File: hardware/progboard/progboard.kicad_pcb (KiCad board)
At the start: 2 copper layers, 74.9 x 58.4 mm, 23 parts, among them J1 LEFT, J2 RIGHT, J3 SWD, J4 CV A, J5 POWER

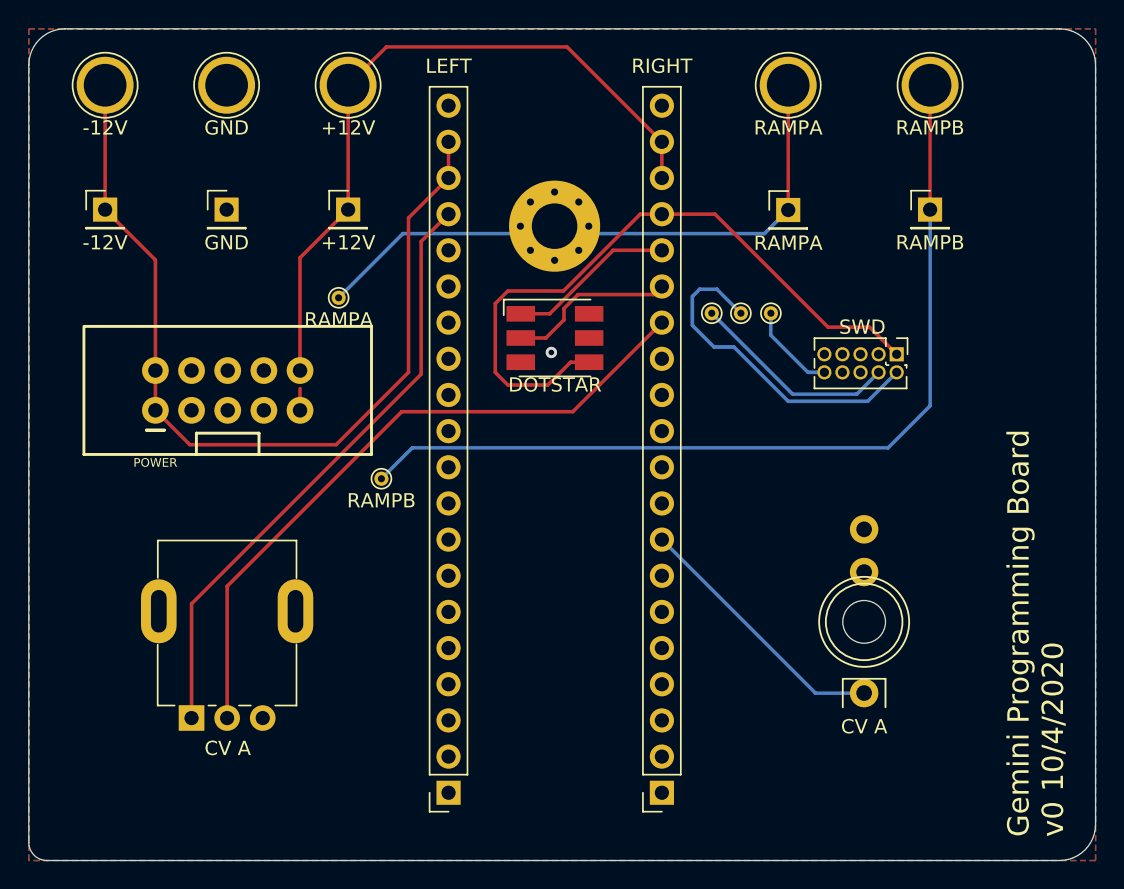
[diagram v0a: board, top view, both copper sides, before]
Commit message: Add LEDs to the progboard
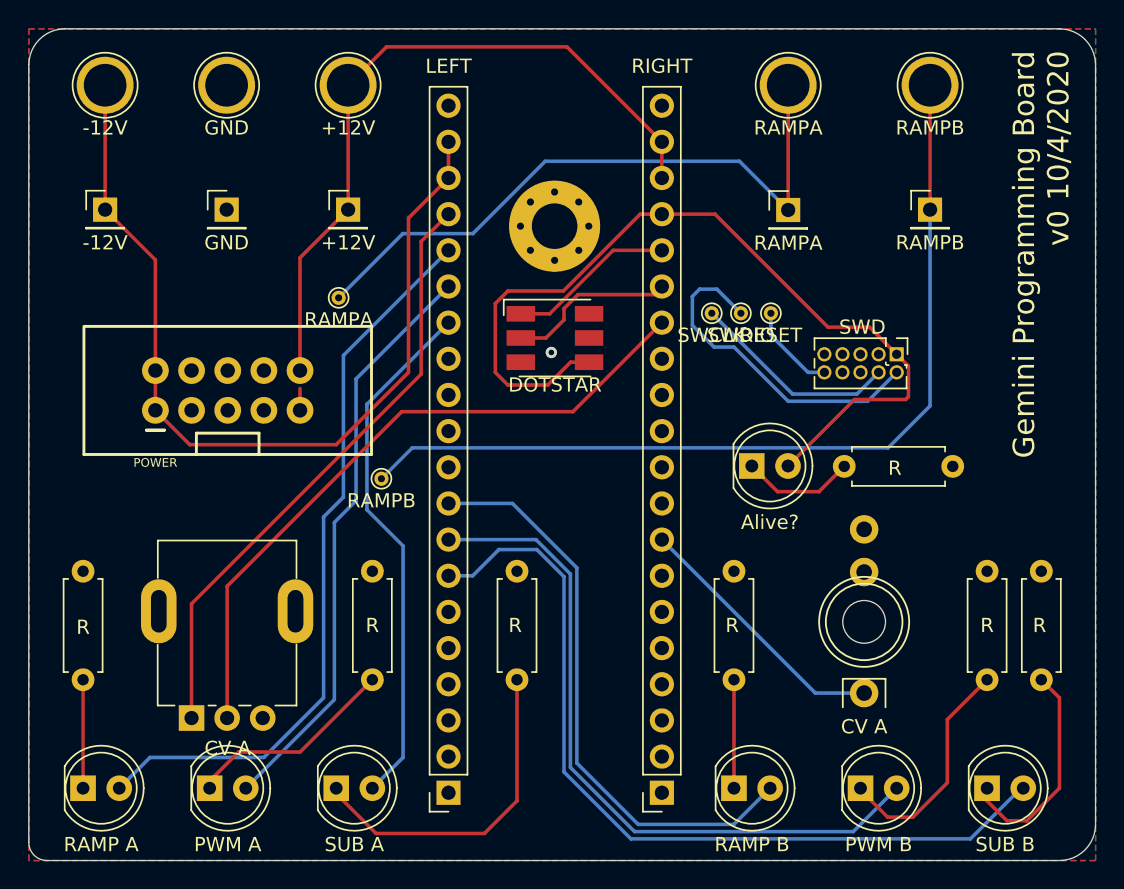
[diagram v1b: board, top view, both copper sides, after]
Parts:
- added 1k1: R, Resistor_THT:R_Axial_DIN0207_L6.3mm_D2.5mm_P7.62mm_Horizontal, F.Cu at (119.4, 108.0)
- added 1k2: R, Resistor_THT:R_Axial_DIN0207_L6.3mm_D2.5mm_P7.62mm_Horizontal, F.Cu at (139.7, 108.0)
- added 1k3: R, Resistor_THT:R_Axial_DIN0207_L6.3mm_D2.5mm_P7.62mm_Horizontal, F.Cu at (149.9, 108.0)
- added 1k4: R, Resistor_THT:R_Axial_DIN0207_L6.3mm_D2.5mm_P7.62mm_Horizontal, F.Cu at (165.1, 108.0)
- added 1k5: R, Resistor_THT:R_Axial_DIN0207_L6.3mm_D2.5mm_P7.62mm_Horizontal, F.Cu at (182.9, 108.0)
- added 1k6: R, Resistor_THT:R_Axial_DIN0207_L6.3mm_D2.5mm_P7.62mm_Horizontal, F.Cu at (186.7, 108.0)
- added 1k7: R, Resistor_THT:R_Axial_DIN0207_L6.3mm_D2.5mm_P7.62mm_Horizontal, F.Cu at (172.8, 93.0)
- added D2: RAMP A, LED_THT:LED_D5.0mm, F.Cu at (119.4, 115.6)
- added D3: PWM A, LED_THT:LED_D5.0mm, F.Cu at (128.3, 115.6)
- added D4: SUB A, LED_THT:LED_D5.0mm, F.Cu at (137.2, 115.6)
- added D5: RAMP B, LED_THT:LED_D5.0mm, F.Cu at (165.1, 115.6)
- added D6: PWM B, LED_THT:LED_D5.0mm, F.Cu at (174.0, 115.6)
- added D7: SUB B, LED_THT:LED_D5.0mm, F.Cu at (182.9, 115.6)
- added D8: Alive?, LED_THT:LED_D5.0mm, F.Cu at (166.4, 92.9)
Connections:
- J1 pad 14: Net-(J1-Pad14) -> /pollux_sub
- J1 pad 15: Net-(J1-Pad15) -> /pollux_pwm
- J1 pad 16: Net-(J1-Pad16) -> /pollux_ramp
- J1 pad 7: Net-(J1-Pad7) -> /castor_sub
- J1 pad 8: Net-(J1-Pad8) -> /castor_pwm
- J1 pad 9: Net-(J1-Pad9) -> /castor_ramp
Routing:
- net /castor_sub: track 0.00 -> 59.1 mm
- net /pollux_ramp: track 0.00 -> 52.0 mm
- net /castor_pwm: track 0.00 -> 49.2 mm
- net /pollux_pwm: track 0.00 -> 41.1 mm
- net /castor_ramp: track 0.00 -> 41.0 mm
- net /pollux_sub: track 0.00 -> 37.0 mm
- net Net-(1k3-Pad1): track 0.00 -> 23.7 mm
- net Net-(1k5-Pad1): track 0.00 -> 16.4 mm
- net Net-(1k6-Pad1): track 0.00 -> 15.6 mm
- net Net-(1k2-Pad1): track 0.00 -> 14.9 mm
- net +3V3: track 47.3 -> 61.1 mm
- net Net-(1k7-Pad1): track 0.00 -> 7.98 mm
- net Net-(1k4-Pad1): track 0.00 -> 7.62 mm
- net Net-(1k1-Pad1): track 0.00 -> 7.62 mm
- net Net-(TP14-Pad1): track 42.9 -> 45.7 mm
